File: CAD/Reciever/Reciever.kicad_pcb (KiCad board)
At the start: 2 copper layers, 193.8 x 67.8 mm, 45 parts, among them J1 Conn_01x02, J2 Output

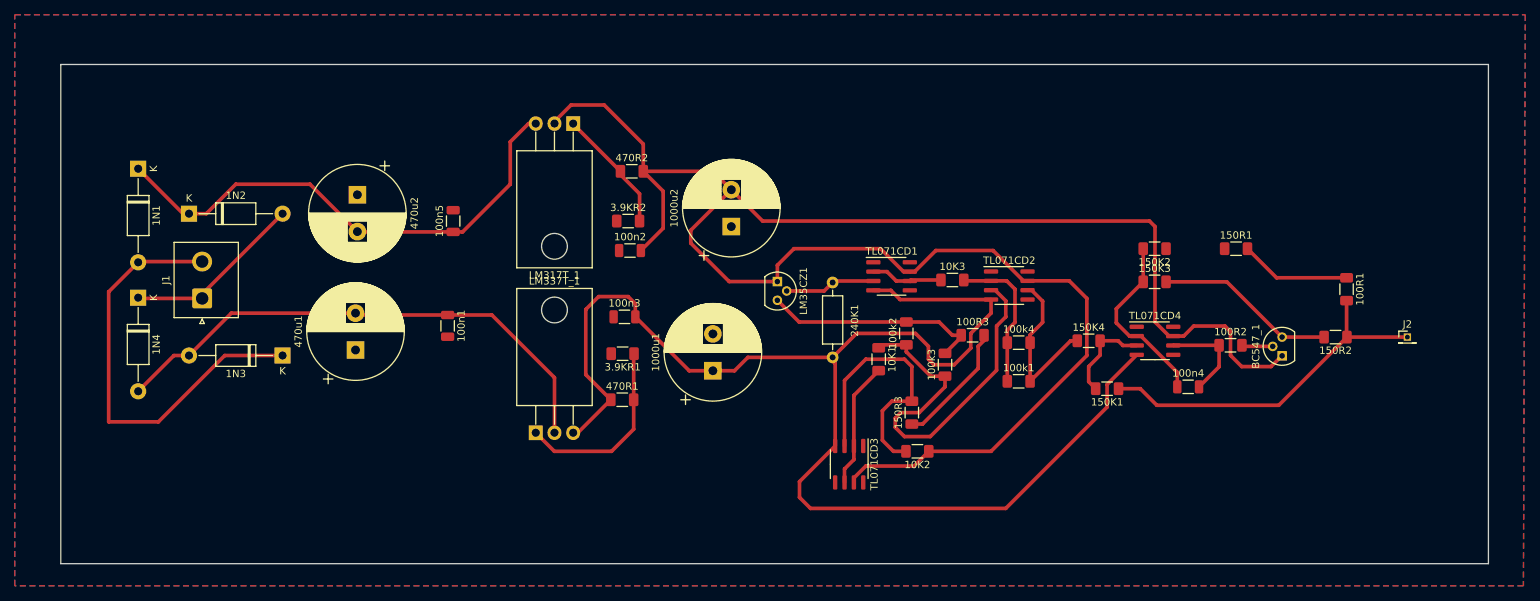
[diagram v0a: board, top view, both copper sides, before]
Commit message: General cleanup, Reciever circuit CAD made
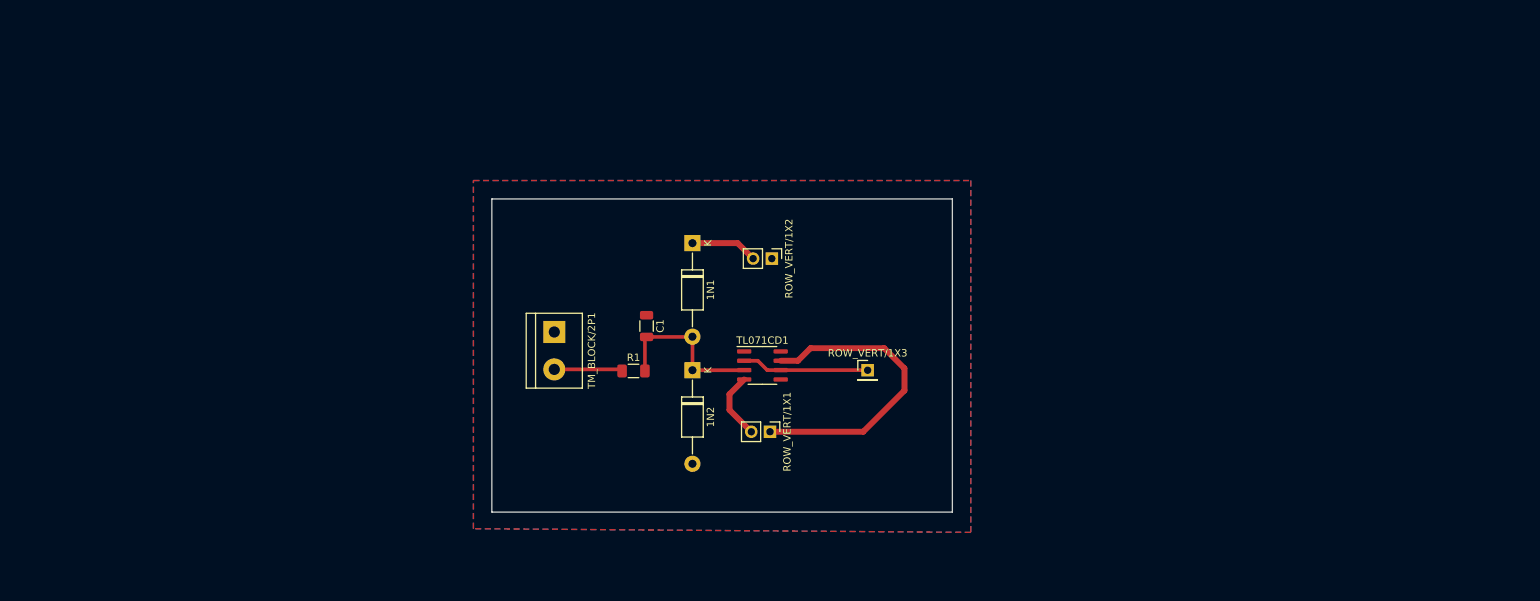
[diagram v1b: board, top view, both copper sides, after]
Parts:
- removed 1000u1, 1000u2: 1000UF_50V_ELE, VAMK_C:C_P_5_0_13
- removed 100R1, 100R2, 100R3: 100R, VAMK_R_SMD:1206
- removed 100k1, 100k2, 100k3, 100k4: 100k, VAMK_R_SMD:1206
- removed 100n1, 100n2, 100n3, 100n4, 100n5: 100NF_50V_CER, VAMK_C_SMD:C1206
- removed 10K1, 10K2, 10K3: 10k, VAMK_R_SMD:1206
- removed 150K1, 150K2, 150K3, 150K4: 150k, VAMK_R_SMD:1206
- removed 150R1, 150R2, 150R3: 150R, VAMK_R_SMD:1206
- removed 1N3, 1N4: 1N4007, VAMK_D:DO41
- removed 240K1: 240k, VAMK_R:R3_5W
- removed 3.9KR1, 3.9KR2: 3.9k, VAMK_R_SMD:1206
- removed 470R1, 470R2: 470R, VAMK_R_SMD:1206
- removed 470u1, 470u2: 470UF_50V_ELE, VAMK_C:C_P_5_0_13
- removed BC547_1: BC547_TO92_0.1A, VAMK_ANA:TO-92
- removed J1: Conn_01x02, Connector_JST:JST_NV_B02P-NV_1x02_P5.00mm_Vertical
- removed J2: Output, Connector_PinHeader_1.27mm:PinHeader_1x01_P1.27mm_Vertical
- removed LM317T_1: LM317T_TO220_1.5A, VAMK_ANA:TO-220
- removed LM337T_1: LM337T_TO220_1.5A, VAMK_ANA:TO-220
- removed LM35CZ1: LM35CZ_TO92, VAMK_IC:TO-92
- removed TL071CD2, TL071CD3, TL071CD4: TL071CD_SO8, VAMK_IC_SMD:SO8IC
- added C1: 10NF_50V_CER, VAMK_C_SMD:C1206, F.Cu at (136.0, 92.2)
- added R1: 100R, VAMK_R_SMD:1206, F.Cu at (134.2, 98.3)
- added ROW_VERT/1X1: ROW_VERT_1X2, VAMK_CON:ROW_VERT_1x2, F.Cu at (152.8, 106.6)
- added ROW_VERT/1X2: ROW_VERT_1X2, VAMK_CON:ROW_VERT_1x2, F.Cu at (153.0, 83.1)
- added ROW_VERT/1X3: ROW_VERT_1X1, VAMK_CON:ROW_VERT_1x1, F.Cu at (166.0, 98.2)
- added TM_BLOCK/2P1: TM_BLOCK_2P, VAMK_CON:TM_BLOCK_2P, F.Cu at (123.5, 93.1)
- 1N1, 1N2: value 1N4007 -> 1N4148
- moved 1N1 75.9 mm to (142.2, 81.0)
- moved 1N2 71.6 mm to (142.2, 98.2), turned to -90 degrees
- moved TL071CD1 21.3 mm to (151.7, 97.6)
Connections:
- 1N2 pad 1: Net-(1N1-K) -> Net-(1N1-A)
- 1N2 pad 2: Net-(1N2-A) -> GND
- TL071CD1 pad 3: Net-(LM35CZ1-Vout) -> Net-(1N1-A)
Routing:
- net Net-(ROW_VERT/1X1-Pin_1): track 261.8 -> 42.2 mm
- net Net-(ROW_VERT/1X1-Pin_2): track 187.1 -> 9.15 mm
- net Net-(1N3-A): track 72.0 -> 0.00 mm
- net Net-(1N1-K): track 71.1 -> 9.10 mm
- net Net-(TL071CD2-+): track 53.2 -> 0.00 mm
- net Net-(J2-Pin_1): track 48.9 -> 0.00 mm
- net Net-(1N1-A): track 59.4 -> 22.5 mm
- net Net-(TL071CD3-+): track 36.7 -> 0.00 mm
- net GND: track 30.3 -> 0.00 mm
- net Net-(LM337T_1-ADJ): track 25.8 -> 0.00 mm
- net Net-(1N2-A): track 24.7 -> 0.00 mm
- net Net-(TL071CD4--): track 24.6 -> 0.00 mm
- net Net-(BC547_1-E): track 24.6 -> 0.00 mm
- net Net-(100k1-Pad2): track 22.9 -> 0.00 mm
- net Net-(TL071CD2--): track 20.4 -> 0.00 mm
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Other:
- board size 193.8 x 67.8 mm -> 62.5 x 42.5 mm
